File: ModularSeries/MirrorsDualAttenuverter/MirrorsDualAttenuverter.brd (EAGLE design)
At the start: 48 x 47 mm, 33 parts, among them IC2 LM358

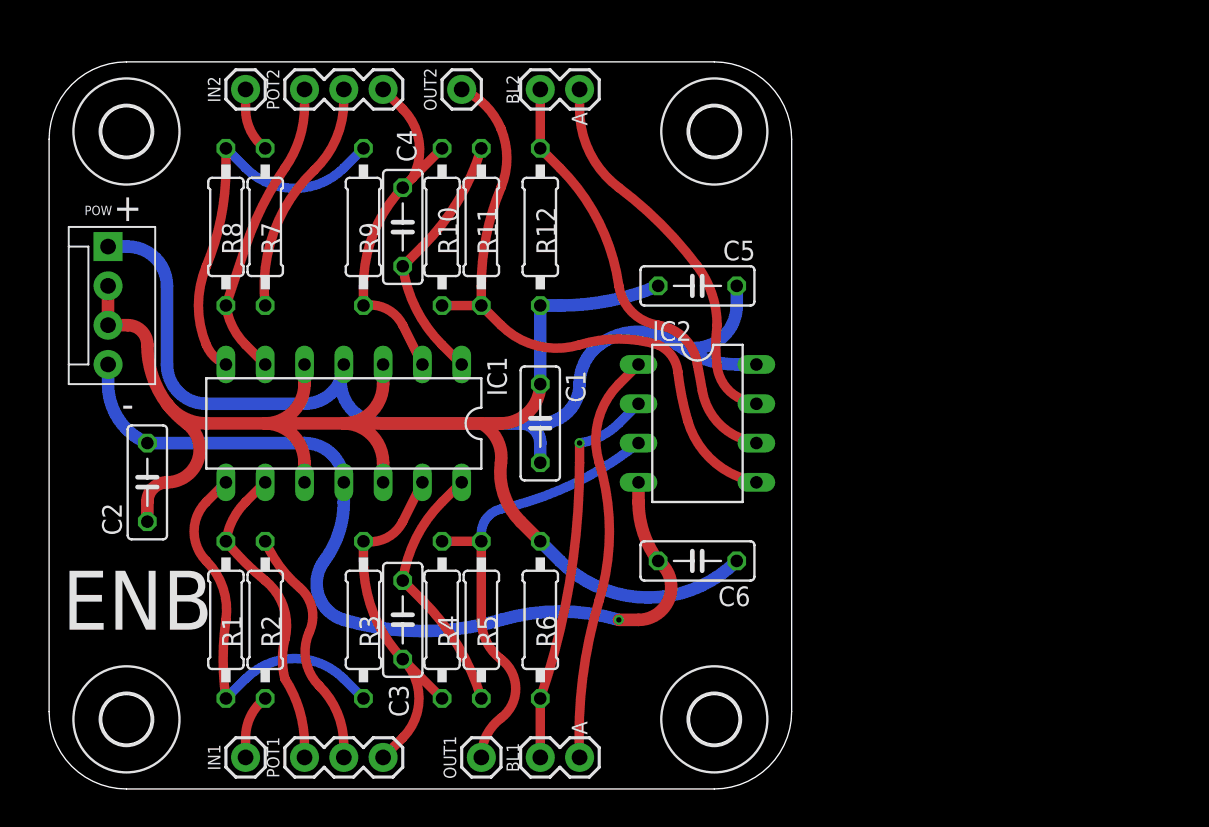
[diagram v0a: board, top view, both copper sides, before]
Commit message: Mirrors Dual Attenuverter DC offset added, layout updated
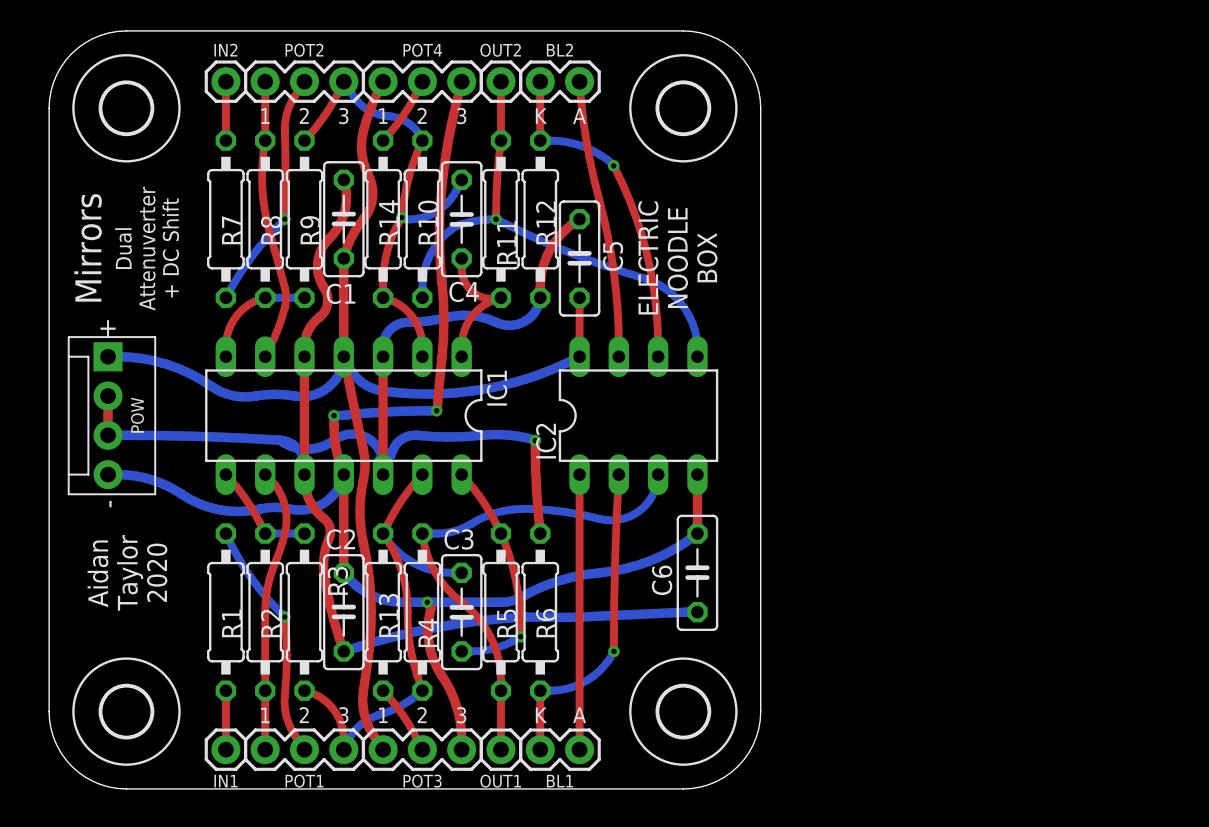
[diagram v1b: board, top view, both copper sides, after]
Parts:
- added POT3, POT4: B100K, ElectricNoodleBox:1X03
- added R13, R14: 100K, rcl:0207/10
- moved H3 54.8 mm to (5.00, 44.0)
- moved H4 53.4 mm to (5.00, 5.00)
- moved H2 36.0 mm to (41.0, 44.0)
- moved H1 36.0 mm to (41.0, 5.00), turned to 0 degrees
- moved C1 18.3 mm to (19.1, 36.8)
- moved C2 15.2 mm to (19.1, 11.4)
- moved C5 7.82 mm to (34.3, 34.3), turned to 90 degrees
- moved POW 7.12 mm to (3.81, 27.9)
- moved C3 3.84 mm to (26.7, 11.4), turned to 270 degrees
- moved C4 3.84 mm to (26.7, 36.8)
- moved R3 3.84 mm to (16.5, 11.4), turned to 270 degrees
- moved R9 3.84 mm to (16.5, 36.8), turned to 90 degrees
- moved IC2 3.84 mm to (38.1, 24.1), turned to 0 degrees
- moved POT1 2.59 mm to (14.0, 2.54)
- moved POT2 2.59 mm to (14.0, 45.7)
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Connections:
- new net N$20: POT3.2, R13.1
- new net N$22: POT4.2, R14.1
- net +12V: now also POT3.1, POT4.1
- net -12V: now also POT3.3, POT4.3
- net N$13: now also R14.2
- net N$5: now also R13.2
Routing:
- net -12V: track 57.3 -> 92.2 mm, vias 1 -> 3
- net AGND: track 98.1 -> 121.0 mm, vias 0 -> 1
- net N$4: track 24.6 -> 7.13 mm
- net N$12: track 24.6 -> 7.24 mm
- net +12V: track 63.9 -> 81.0 mm
- net N$8: track 26.2 -> 17.8 mm
- net N$15: track 16.7 -> 8.51 mm
- net N$14: track 41.2 -> 33.2 mm, vias 0 -> 1
- net N$5: track 24.3 -> 32.0 mm
- net N$13: track 23.7 -> 31.0 mm, vias 0 -> 1
- net N$17: track 24.4 -> 18.0 mm
- net N$18: track 28.0 -> 21.6 mm, vias 0 -> 1
- net N$22: track 0.00 -> 4.59 mm
- net N$20: track 0.00 -> 4.59 mm
- net N$19: track 25.2 -> 20.7 mm
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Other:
- board size 48 x 47 mm -> 46 x 49 mm
- board text added: "1"
- board text added: "2"
- board text added: "3"
- board text added: "Dual Attenuverter + DC Shift"
- board text added: "K"
- board text added: "Mirrors"
- board text removed: "Dual Attenuverter"
- board text removed: "ENB"

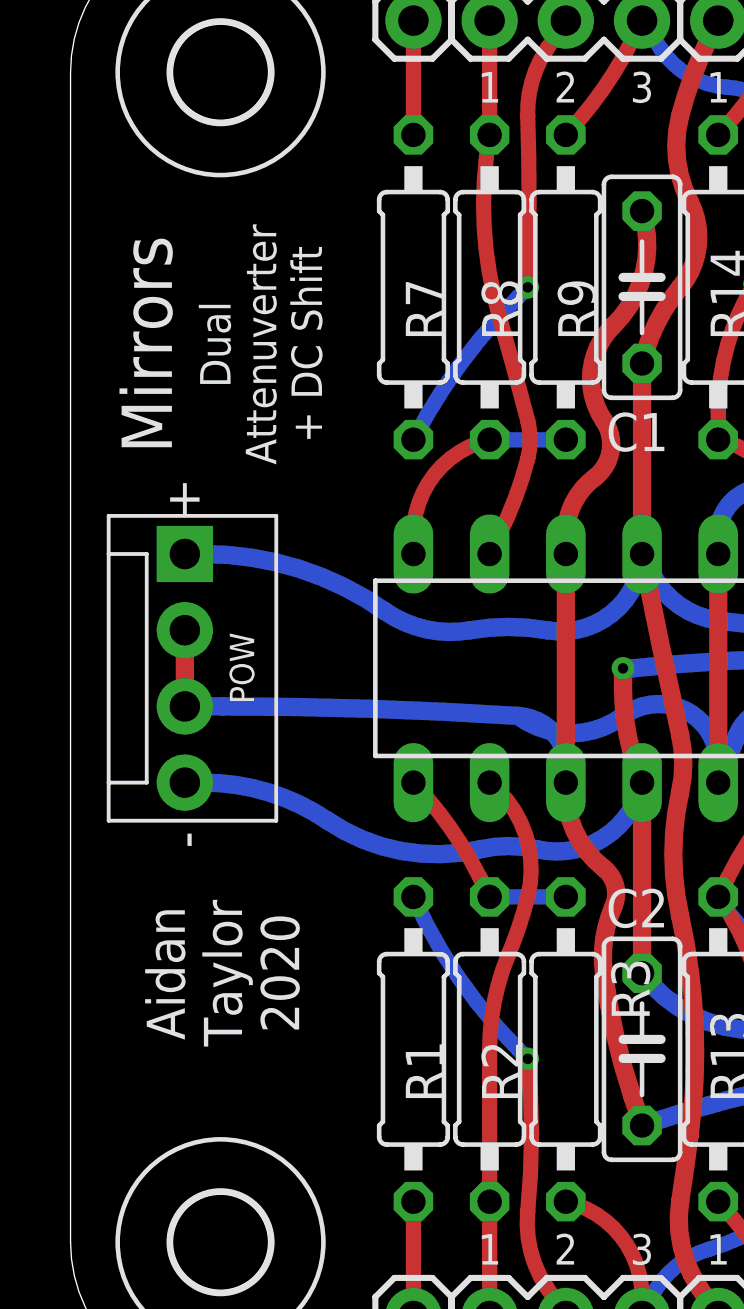
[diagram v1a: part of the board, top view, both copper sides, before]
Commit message: Power header updated on most PCBs. Knives layout added
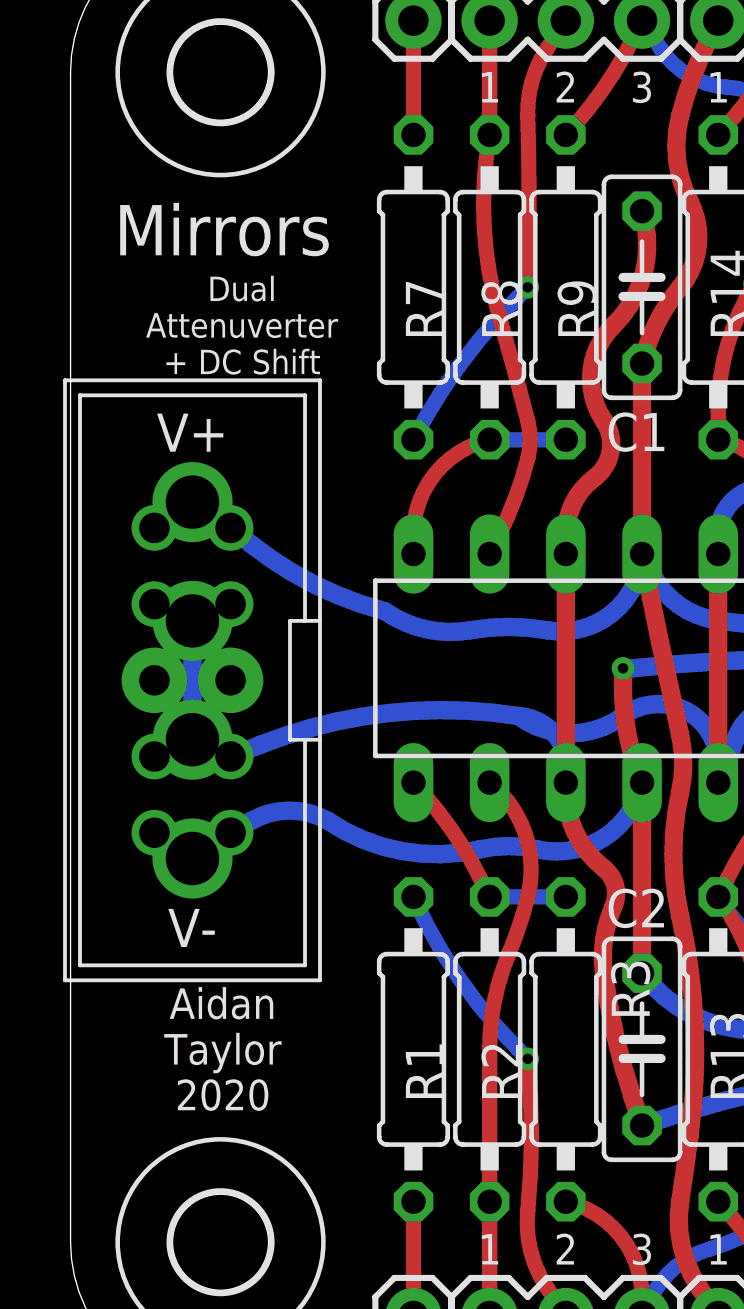
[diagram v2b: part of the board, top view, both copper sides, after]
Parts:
- removed POW: 4XMOLEX, ElectricNoodleBox:MOLEX-1X4
- added WP1: COMBO_SUPPLY_HEADER, ElectricNoodleBox:COMBINED_POWER
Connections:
- net +12V: now also WP1.V+1, WP1.V+2, WP1.V+3; no longer POW.1
- net -12V: now also WP1.V-1, WP1.V-2, WP1.V-3; no longer POW.4
- net AGND: now also WP1.GND1, WP1.GND2, WP1.GND3, WP1.GND4, WP1.GND5, WP1.GND6, WP1.GND7, WP1.GND8; no longer POW.2, POW.3
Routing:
- net AGND: track 121.0 -> 129.1 mm
- net +12V: track 81.0 -> 82.9 mm
- net -12V: track 92.2 -> 93.7 mm
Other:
- board text removed: "+"
- board text removed: "-"
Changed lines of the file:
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@@
 <setting verticaltext="up"/>
 </settings>
-<grid distance="1" unitdist="mm" unit="mm" style="lines" multiple="1" display="no" altdistance="5" altunitdist="mil" altunit="mil"/>
+<grid distance="12.5" unitdist="mil" unit="mil" style="lines" multiple="1" display="yes" altdistance="5" altunitdist="mil" altunit="mil"/>
 <layers>
 <layer number="1" name="Top" color="4" fill="1" visible="yes" active="yes"/>
@@
 NOODLE
 BOX</text>
-<text x="5.08" y="13.97" size="1.27" layer="21" font="vector" ratio="16" rot="R90" align="center">Aidan
+<text x="5.08" y="11.43" size="1.016" layer="21" font="vector" ratio="16" rot="R180" align="center">Aidan
 Taylor
 2020</text>
-<text x="2.54" y="34.925" size="1.6764" layer="21" font="vector" ratio="16" rot="R90" align="center">Mirrors</text>
-<text x="6.35" y="34.925" size="1.016" layer="21" font="vector" ratio="16" rot="R90" align="center">Dual
+<text x="5.08" y="38.735" size="1.6764" layer="21" font="vector" ratio="16" rot="R180" align="center">Mirrors</text>
+<text x="5.715" y="35.56" size="0.8128" layer="21" font="vector" ratio="16" rot="R180" align="center">Dual
 Attenuverter
 + DC Shift</text>
@@
 <text x="31.75" y="43.4975" size="1.016" layer="21" font="vector" ratio="16" align="center">K</text>
 <text x="34.29" y="43.4975" size="1.016" layer="21" font="vector" ratio="16" align="center">A</text>
-<text x="3.81" y="29.845" size="1.27" layer="21" font="vector" ratio="16" align="center">+</text>
-<text x="3.81" y="18.415" size="1.27" layer="21" font="vector" ratio="16" rot="R90" align="center">-</text>
 <dimension x1="5" y1="5" x2="41" y2="5" x3="23" y3="-2" textsize="1.016" textratio="16" layer="21"/>
 <dimension x1="0" y1="0" x2="46" y2="0" x3="23" y3="-4" textsize="1.016" textratio="16" layer="21"/>
@@
 <attribute name="VALUE" x="22.225" y="47.498" size="0.6096" layer="27" font="vector" ratio="20"/>
 </element>
-<element name="POW" library="ElectricNoodleBox" package="MOLEX-1X4" value="4XMOLEX" x="3.81" y="27.94" smashed="yes" rot="R270">
-<attribute name="NAME" x="5.715" y="24.13" size="0.8128" layer="25" font="vector" ratio="20" rot="R270" align="center"/>
-<attribute name="VALUE" x="0.381" y="25.654" size="0.6096" layer="27" font="vector" ratio="20" rot="R270"/>
-</element>
 <element name="R1" library="rcl" library_urn="urn:adsk.eagle:library:334" package="0207/10" package3d_urn="urn:adsk.eagle:package:23491/2" value="100K" x="11.43" y="11.43" smashed="yes" rot="R90">
 <attribute name="NAME" x="12.446" y="9.652" size="1.27" layer="25" ratio="10" rot="R90"/>
@@
 <attribute name="VALUE" x="17.145" y="34.5694" size="1.27" layer="27" ratio="10" rot="R90"/>
 </element>
+<element name="WP1" library="ElectricNoodleBox" package="COMBINED_POWER" value="COMBO_SUPPLY_HEADER" x="4.065" y="23.73" smashed="yes" rot="R270"/>
 </elements>
 <signals>
@@
 <contactref element="C5" pad="2"/>
 <contactref element="C6" pad="1"/>
-<contactref element="POW" pad="3"/>
-<contactref element="POW" pad="2"/>
 <wire x1="19.05" y1="8.89" x2="18.7325" y2="9.8425" width="0.6096" layer="1"/>
 <wire x1="18.7325" y1="9.8425" x2="17.78" y2="13.97" width="0.6096" layer="1" curve="-10.880664"/>
@@
 <wire x1="30.7975" y1="11.1125" x2="19.05" y2="8.89" width="0.6096" layer="16" curve="15.837578"/>
 <wire x1="21.59" y1="20.32" x2="21.59" y2="27.94" width="0.6096" layer="1"/>
-<wire x1="3.81" y1="22.86" x2="5.08" y2="22.86" width="0.6096" layer="16"/>
-<wire x1="5.08" y1="22.86" x2="14.9225" y2="22.5425" width="0.6096" layer="16" curve="-3.695221"/>
 <wire x1="16.51" y1="20.32" x2="14.9225" y2="22.5425" width="0.6096" layer="16" curve="101.534288"/>
 <wire x1="21.59" y1="20.32" x2="21.59" y2="20.955" width="0.6096" layer="16"/>
@@
 <wire x1="16.51" y1="27.94" x2="16.51" y2="20.32" width="0.6096" layer="1"/>
 <wire x1="33.715403125" y1="11.084621875" x2="30.7975" y2="11.1125" width="0.6096" layer="16"/>
-<wire x1="3.81" y1="25.4" x2="3.81" y2="22.86" width="0.6096" layer="1"/>
 <wire x1="21.59" y1="27.94" x2="21.59" y2="28.575" width="0.6096" layer="16"/>
 <wire x1="21.59" y1="28.575" x2="23.1775" y2="30.1625" width="0.6096" layer="16" curve="-90"/>
@@
 <wire x1="31.75" y1="31.75" x2="31.75" y2="32.385" width="0.6096" layer="1"/>
 <wire x1="31.75" y1="32.385" x2="34.29" y2="36.83" width="0.6096" layer="1" curve="-59.489763"/>
+<contactref element="WP1" pad="GND1"/>
+<contactref element="WP1" pad="GND4"/>
+<contactref element="WP1" pad="GND8"/>
+<contactref element="WP1" pad="GND6"/>
+<contactref element="WP1" pad="GND2"/>
+<contactref element="WP1" pad="GND5"/>
+<contactref element="WP1" pad="GND7"/>
+<contactref element="WP1" pad="GND3"/>
+<wire x1="4.065" y1="21.75" x2="5.335" y2="21.19" width="0.6096" layer="16"/>
+<wire x1="4.065" y1="21.75" x2="2.795" y2="21.19" width="0.6096" layer="16"/>
+<wire x1="5.335" y1="21.19" x2="6.35" y2="21.59" width="0.6096" layer="16"/>
+<wire x1="6.35" y1="21.59" x2="14.9225" y2="22.5425" width="0.6096" layer="16" curve="-30.337294"/>
+<wire x1="2.795" y1="23.73" x2="5.335" y2="23.73" width="0.6096" layer="16"/>
+<wire x1="4.065" y1="25.71" x2="4.065" y2="21.75" width="0.6096" layer="16"/>
+<wire x1="4.065" y1="25.71" x2="5.335" y2="26.27" width="0.6096" layer="16"/>
+<wire x1="2.795" y1="26.27" x2="4.065" y2="25.71" width="0.6096" layer="16"/>
+<wire x1="4.065" y1="25.71" x2="5.335" y2="23.73" width="0" layer="19" extent="1-1"/>
 </signal>
 <signal name="N$4">
@@
 <contactref element="C5" pad="1"/>
 <contactref element="C1" pad="1"/>
-<contactref element="POW" pad="1"/>
 <contactref element="IC2" pad="8"/>
 <contactref element="POT3" pad="1"/>
@@
 <wire x1="20.32" y1="20.0025" x2="20.32" y2="21.9075" width="0.6096" layer="1" curve="25.213833"/>
 <wire x1="20.32" y1="21.9075" x2="19.05" y2="27.94" width="0.6096" layer="1" curve="-1.436522"/>
-<wire x1="3.81" y1="27.94" x2="4.445" y2="27.94" width="0.6096" layer="16"/>
-<wire x1="4.445" y1="27.94" x2="10.4775" y2="26.035" width="0.6096" layer="16" curve="-35.051133"/>
 <wire x1="10.4775" y1="26.035" x2="13.335" y2="25.4" width="0.6096" layer="16" curve="45.04462"/>
 <wire x1="13.335" y1="25.4" x2="15.875" y2="25.4" width="0.6096" layer="16" curve="-19.986957"/>
@@
 <wire x1="27.305" y1="25.7175" x2="34.29" y2="27.94" width="0.6096" layer="16" curve="20.019365"/>
 <wire x1="34.29" y1="27.94" x2="34.29" y2="31.75" width="0.508" layer="1"/>
+<contactref element="WP1" pad="V+3"/>
+<contactref element="WP1" pad="V+2"/>
+<contactref element="WP1" pad="V+1"/>
+<wire x1="5.335" y1="28.81" x2="6.0325" y2="28.2575" width="0.6096" layer="16"/>
+<wire x1="6.0325" y1="28.2575" x2="10.4775" y2="26.035" width="0.6096" layer="16" curve="23.636422"/>
+<wire x1="4.065" y1="29.67" x2="5.335" y2="28.81" width="0.6096" layer="16"/>
+<wire x1="4.065" y1="29.67" x2="2.795" y2="28.81" width="0.6096" layer="16"/>
 </signal>
 <signal name="-12V">
@@
 <contactref element="C6" pad="2"/>
 <contactref element="C2" pad="2"/>
-<contactref element="POW" pad="4"/>
 <contactref element="IC2" pad="4"/>
 <contactref element="POT3" pad="3"/>
@@
 <wire x1="22.86" y1="12.065" x2="19.05" y2="13.97" width="0.6096" layer="16" curve="-53.130102"/>
 <wire x1="24.4475" y1="12.065" x2="29.28470625" y2="12.065" width="0.6096" layer="16"/>
-<wire x1="3.81" y1="20.32" x2="4.445" y2="20.32" width="0.6096" layer="16"/>
-<wire x1="4.445" y1="20.32" x2="8.5725" y2="19.05" width="0.6096" layer="16" curve="-34.205458"/>
 <wire x1="8.5725" y1="19.05" x2="13.6525" y2="18.0975" width="0.6096" layer="16" curve="47.171581"/>
 <wire x1="13.6525" y1="18.0975" x2="15.5575" y2="18.0975" width="0.6096" layer="16" curve="-25.932253"/>
@@
 <wire x1="35.56" y1="13.97" x2="41.91" y2="16.51" width="0.6096" layer="16" curve="33.689405"/>
 <wire x1="41.91" y1="16.51" x2="41.91" y2="20.32" width="0.6096" layer="1"/>
+<contactref element="WP1" pad="V-2"/>
+<contactref element="WP1" pad="V-3"/>
+<contactref element="WP1" pad="V-1"/>
+<wire x1="5.335" y1="18.65" x2="6.0325" y2="19.05" width="0.6096" layer="16"/>
+<wire x1="6.0325" y1="19.05" x2="8.5725" y2="19.05" width="0.6096" layer="16" curve="-59.666533"/>
+<wire x1="4.065" y1="17.79" x2="5.335" y2="18.65" width="0.6096" layer="16"/>
+<wire x1="4.065" y1="17.79" x2="2.795" y2="18.65" width="0.6096" layer="16"/>
 </signal>
 <signal name="N$19">
